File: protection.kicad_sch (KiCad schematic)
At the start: 20 parts, among them Q1 SQJQ184ER, Q2 SQJQ184ER, Q3 SQJQ184ER, Q4 SQJQ184ER

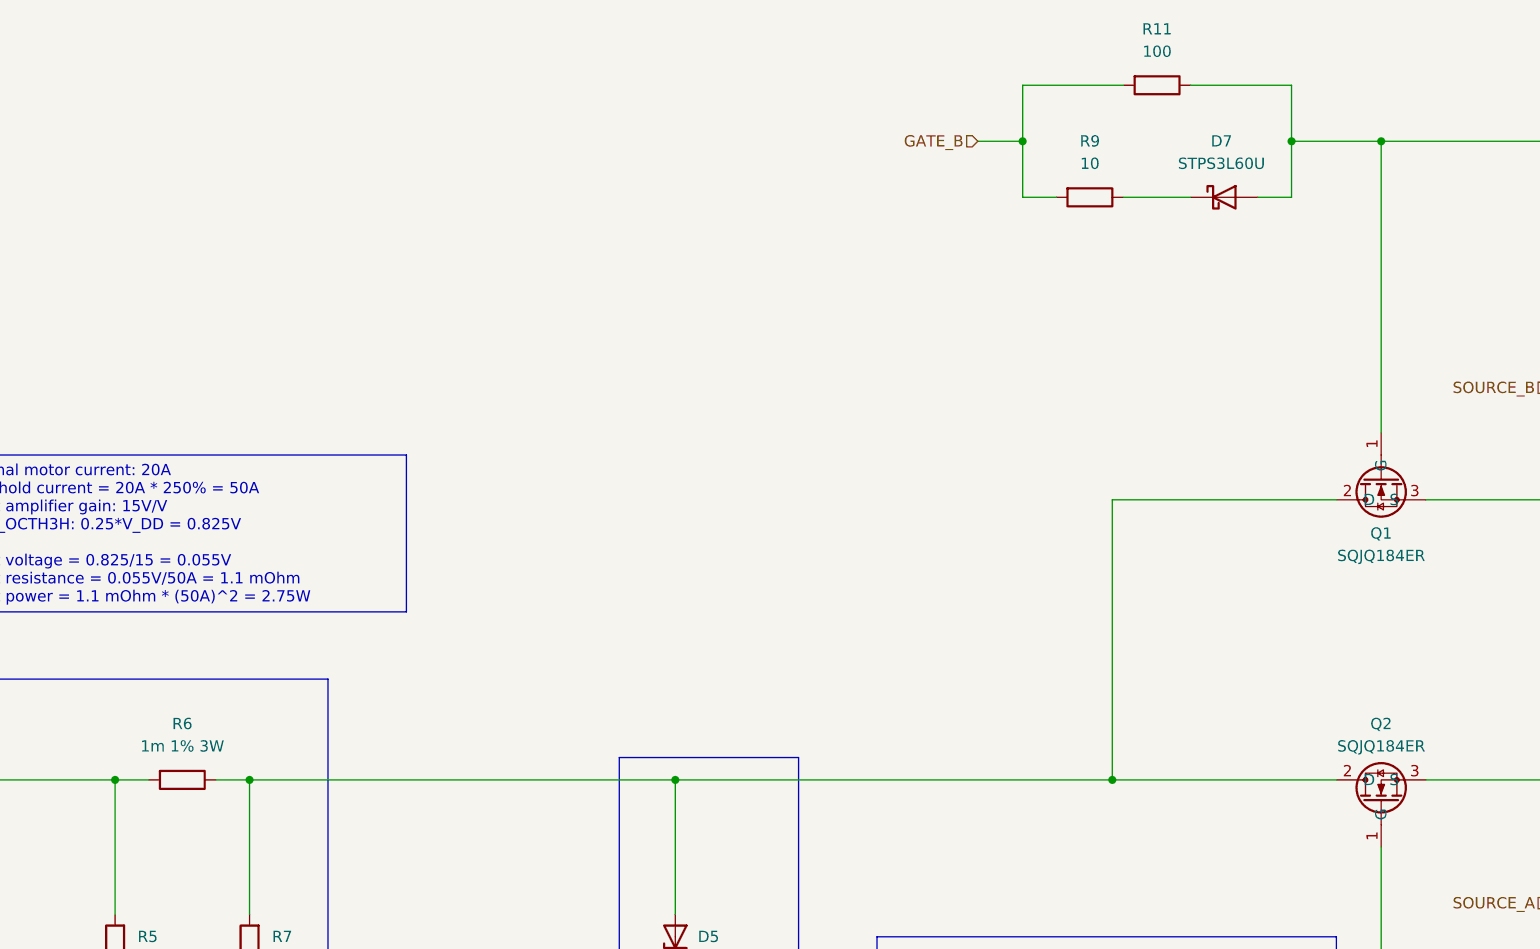
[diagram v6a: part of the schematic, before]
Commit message: Updated pcb rules and started the rough routing of protection circuitry (#5)
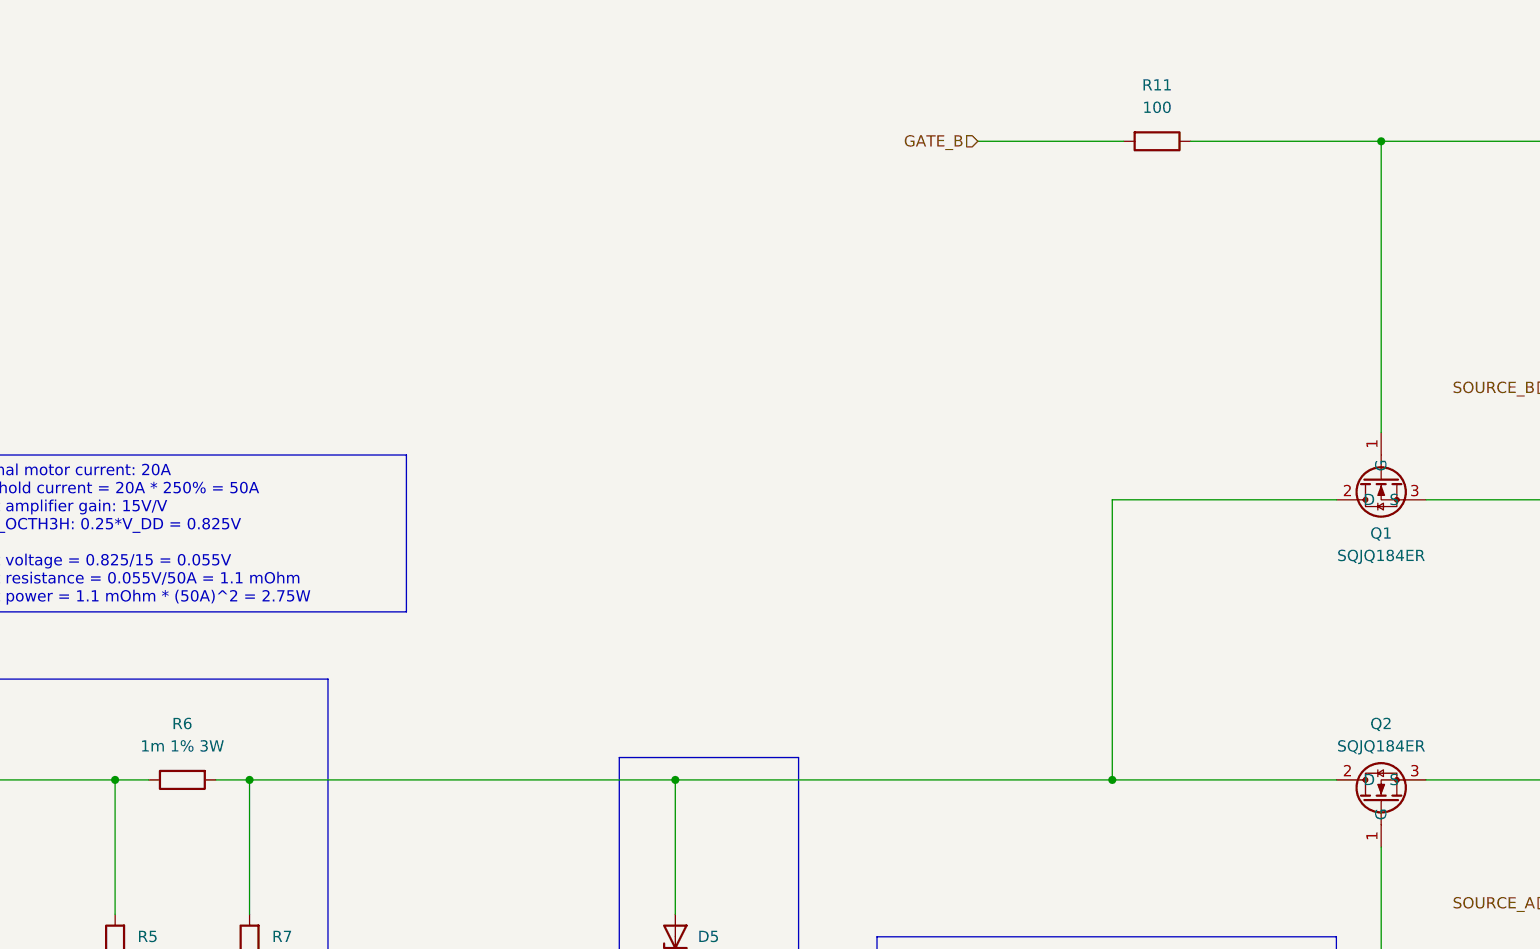
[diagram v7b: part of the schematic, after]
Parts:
- removed D7: STPS3L60U, custom_footprints:STPS3L60U, symbol Device:D_Schottky
- removed R9: 10, Resistor_SMD:R_0603_1608Metric, symbol Device:R
- R14: footprint Resistor_SMD:R_0603_1608Metric -> Resistor_SMD:R_1206_3216Metric
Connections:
- net BAT+: now also R6.1; no longer R6.2
- net at D5.1 (A1), Q1.2 (D), Q2.2 (D)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: now also R6.2; no longer R6.1
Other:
- moved on the sheet: R11, R6

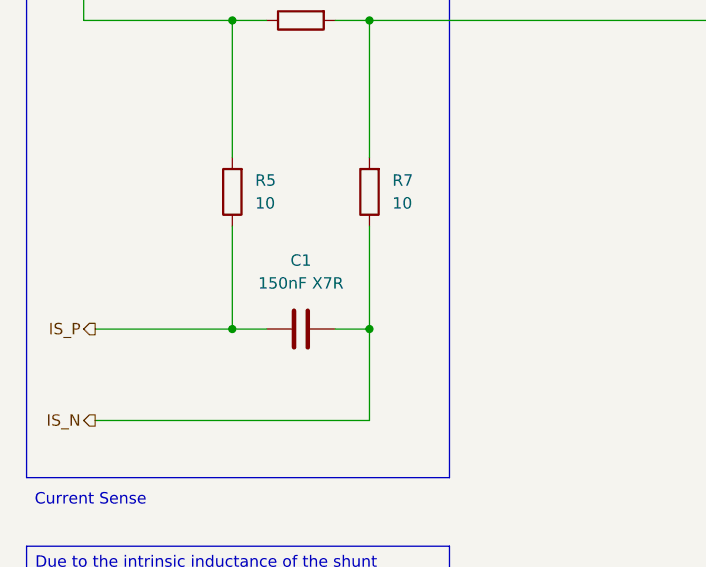
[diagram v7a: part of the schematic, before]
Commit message: More routing, changed the footprints of some caps.
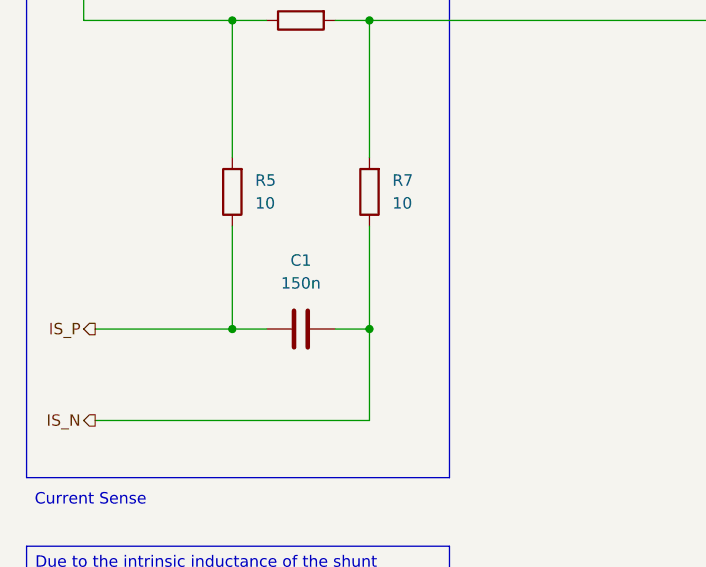
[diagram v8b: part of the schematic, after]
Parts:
- C1: value 150nF X7R -> 150n
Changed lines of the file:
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@@
 			)
 		)
-		(property "Value" "150nF X7R"
+		(property "Value" "150n"
 			(at 63.5 151.13 90)
 			(effects
